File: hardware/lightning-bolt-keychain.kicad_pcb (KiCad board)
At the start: 2 copper layers, 74 x 101 mm, 15 parts, among them J1 USB-C Power

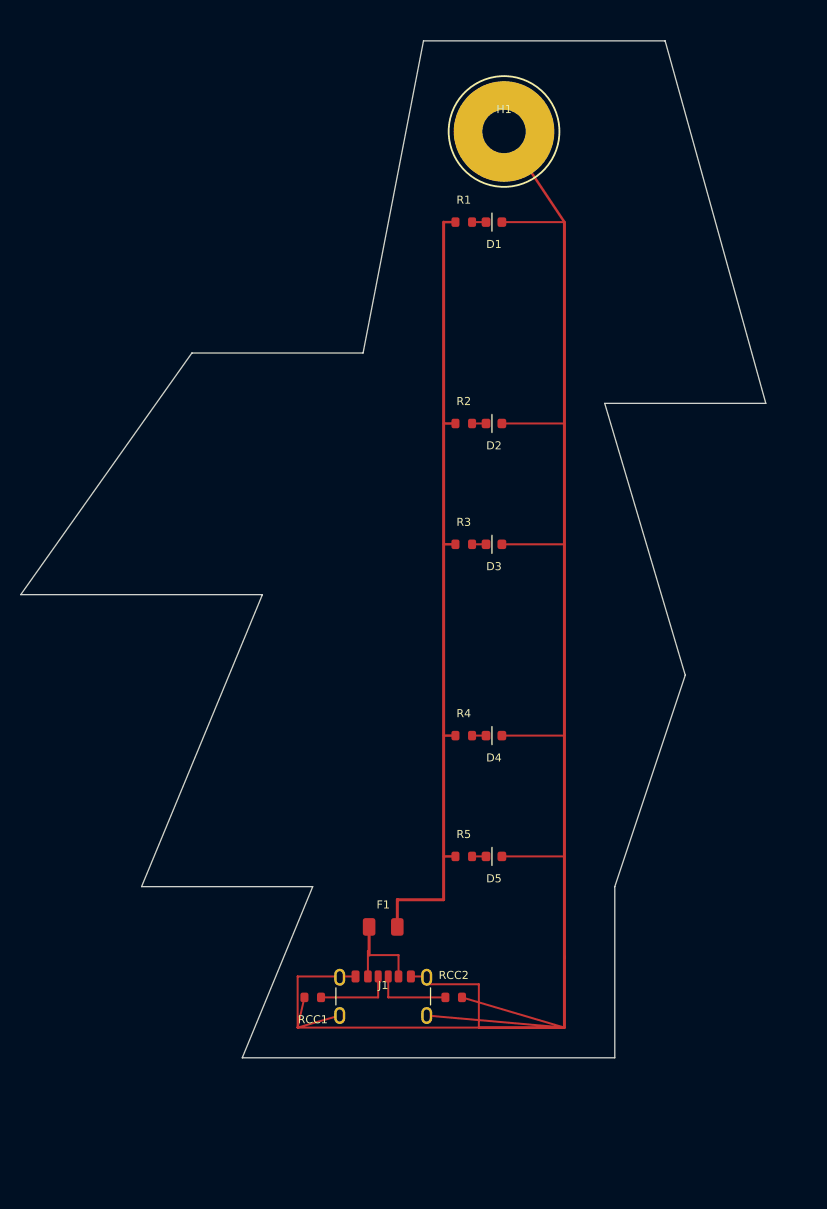
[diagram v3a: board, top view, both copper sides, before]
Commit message: Refine bolt outline and schematic readability
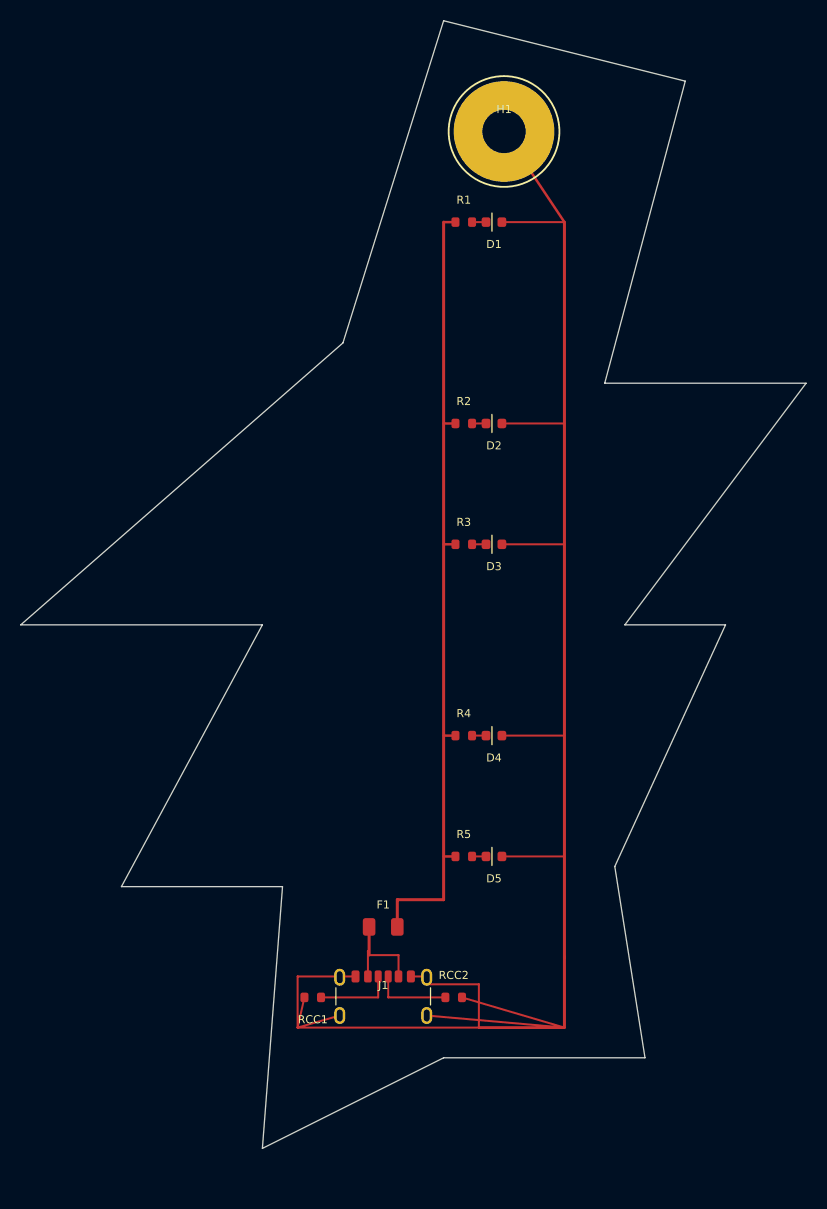
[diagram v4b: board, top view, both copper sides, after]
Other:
- board size 74 x 101 mm -> 78 x 112 mm
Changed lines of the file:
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@@
     (pad "2" smd roundrect (at 0.7875 0) (size 0.875 0.95) (layers "F.Cu" "F.Paste" "F.Mask") (net 10 "LED5") (pinfunction "A") (roundrect_rratio 0.25))
   )
-  (gr_line (start 86 20) (end 110 20) (stroke (width 0.12) (type solid)) (layer "Edge.Cuts"))
-  (gr_line (start 110 20) (end 120 56) (stroke (width 0.12) (type solid)) (layer "Edge.Cuts"))
-  (gr_line (start 120 56) (end 104 56) (stroke (width 0.12) (type solid)) (layer "Edge.Cuts"))
-  (gr_line (start 104 56) (end 112 83) (stroke (width 0.12) (type solid)) (layer "Edge.Cuts"))
-  (gr_line (start 112 83) (end 105 104) (stroke (width 0.12) (type solid)) (layer "Edge.Cuts"))
-  (gr_line (start 105 104) (end 105 121) (stroke (width 0.12) (type solid)) (layer "Edge.Cuts"))
-  (gr_line (start 105 121) (end 68 121) (stroke (width 0.12) (type solid)) (layer "Edge.Cuts"))
-  (gr_line (start 68 121) (end 75 104) (stroke (width 0.12) (type solid)) (layer "Edge.Cuts"))
-  (gr_line (start 75 104) (end 58 104) (stroke (width 0.12) (type solid)) (layer "Edge.Cuts"))
-  (gr_line (start 58 104) (end 70 75) (stroke (width 0.12) (type solid)) (layer "Edge.Cuts"))
-  (gr_line (start 70 75) (end 46 75) (stroke (width 0.12) (type solid)) (layer "Edge.Cuts"))
-  (gr_line (start 46 75) (end 63 51) (stroke (width 0.12) (type solid)) (layer "Edge.Cuts"))
-  (gr_line (start 63 51) (end 80 51) (stroke (width 0.12) (type solid)) (layer "Edge.Cuts"))
-  (gr_line (start 80 51) (end 86 20) (stroke (width 0.12) (type solid)) (layer "Edge.Cuts"))
-  (segment (start 80.48 112.92) (end 80.48 110.4) (width 0.20) (layer "F.Cu") (net 2))
+  (gr_line (start 88 18) (end 112 24) (stroke (width 0.12) (type solid)) (layer "Edge.Cuts"))
+  (gr_line (start 112 24) (end 104 54) (stroke (width 0.12) (type solid)) (layer "Edge.Cuts"))
+  (gr_line (start 104 54) (end 124 54) (stroke (width 0.12) (type solid)) (layer "Edge.Cuts"))
+  (gr_line (start 124 54) (end 106 78) (stroke (width 0.12) (type solid)) (layer "Edge.Cuts"))
+  (gr_line (start 106 78) (end 116 78) (stroke (width 0.12) (type solid)) (layer "Edge.Cuts"))
+  (gr_line (start 116 78) (end 105 102) (stroke (width 0.12) (type solid)) (layer "Edge.Cuts"))
+  (gr_line (start 105 102) (end 108 121) (stroke (width 0.12) (type solid)) (layer "Edge.Cuts"))
+  (gr_line (start 108 121) (end 88 121) (stroke (width 0.12) (type solid)) (layer "Edge.Cuts"))
+  (gr_line (start 88 121) (end 70 130) (stroke (width 0.12) (type solid)) (layer "Edge.Cuts"))
+  (gr_line (start 70 130) (end 72 104) (stroke (width 0.12) (type solid)) (layer "Edge.Cuts"))
+  (gr_line (start 72 104) (end 56 104) (stroke (width 0.12) (type solid)) (layer "Edge.Cuts"))
+  (gr_line (start 56 104) (end 70 78) (stroke (width 0.12) (type solid)) (layer "Edge.Cuts"))
+  (gr_line (start 70 78) (end 46 78) (stroke (width 0.12) (type solid)) (layer "Edge.Cuts"))
+  (gr_line (start 46 78) (end 78 50) (stroke (width 0.12) (type solid)) (layer "Edge.Cuts"))
+  (gr_line (start 78 50) (end 88 18) (stroke (width 0.12) (type solid)) (layer "Edge.Cuts"))  (segment (start 80.48 112.92) (end 80.48 110.4) (width 0.20) (layer "F.Cu") (net 2))
   (segment (start 80.48 110.4) (end 80.6 110.4) (width 0.20) (layer "F.Cu") (net 2))
   (segment (start 83.52 112.92) (end 83.52 110.8) (width 0.20) (layer "F.Cu") (net 2))

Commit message: Refine lightning bolt silhouette
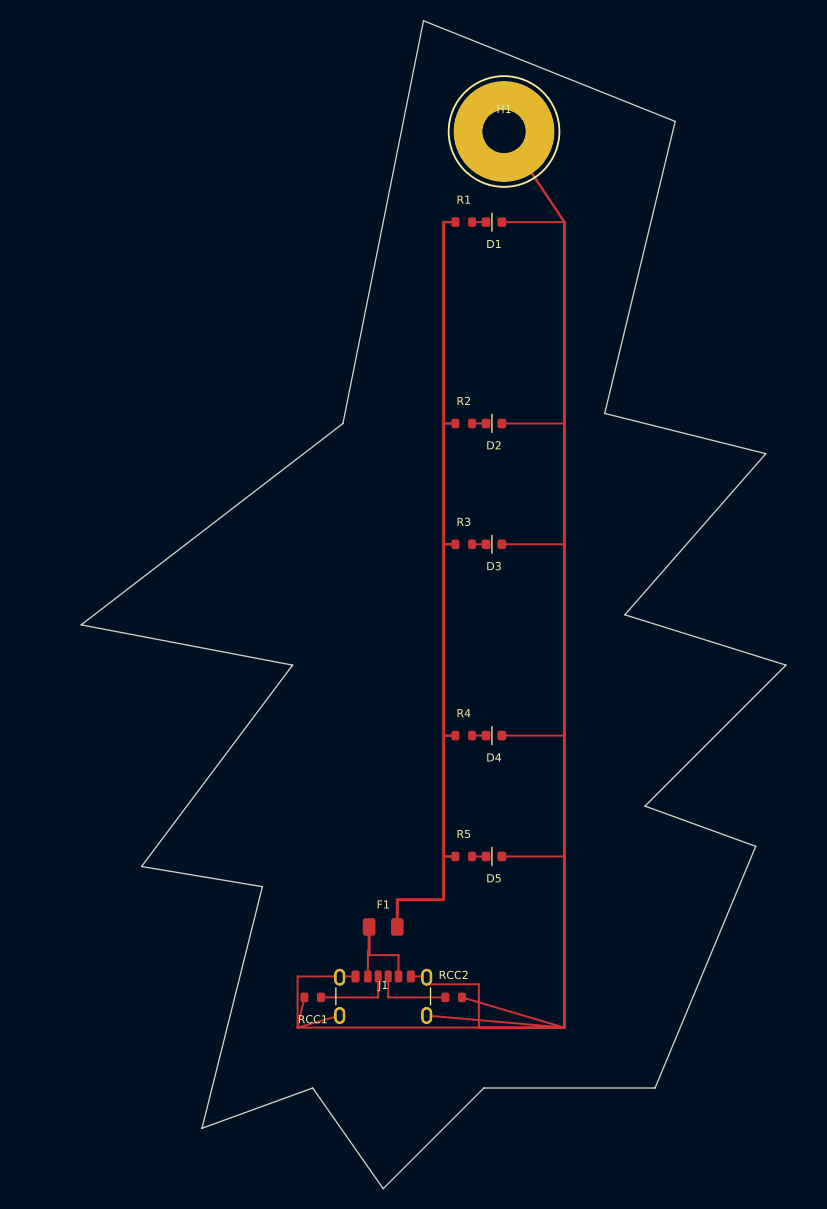
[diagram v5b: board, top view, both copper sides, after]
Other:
- board size 78 x 112 mm -> 70 x 116 mm
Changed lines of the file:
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@@
     (pad "2" smd roundrect (at 0.7875 0) (size 0.875 0.95) (layers "F.Cu" "F.Paste" "F.Mask") (net 10 "LED5") (pinfunction "A") (roundrect_rratio 0.25))
   )
-  (gr_line (start 88 18) (end 112 24) (stroke (width 0.12) (type solid)) (layer "Edge.Cuts"))
-  (gr_line (start 112 24) (end 104 54) (stroke (width 0.12) (type solid)) (layer "Edge.Cuts"))
-  (gr_line (start 104 54) (end 124 54) (stroke (width 0.12) (type solid)) (layer "Edge.Cuts"))
-  (gr_line (start 124 54) (end 106 78) (stroke (width 0.12) (type solid)) (layer "Edge.Cuts"))
-  (gr_line (start 106 78) (end 116 78) (stroke (width 0.12) (type solid)) (layer "Edge.Cuts"))
-  (gr_line (start 116 78) (end 105 102) (stroke (width 0.12) (type solid)) (layer "Edge.Cuts"))
-  (gr_line (start 105 102) (end 108 121) (stroke (width 0.12) (type solid)) (layer "Edge.Cuts"))
-  (gr_line (start 108 121) (end 88 121) (stroke (width 0.12) (type solid)) (layer "Edge.Cuts"))
-  (gr_line (start 88 121) (end 70 130) (stroke (width 0.12) (type solid)) (layer "Edge.Cuts"))
-  (gr_line (start 70 130) (end 72 104) (stroke (width 0.12) (type solid)) (layer "Edge.Cuts"))
-  (gr_line (start 72 104) (end 56 104) (stroke (width 0.12) (type solid)) (layer "Edge.Cuts"))
-  (gr_line (start 56 104) (end 70 78) (stroke (width 0.12) (type solid)) (layer "Edge.Cuts"))
-  (gr_line (start 70 78) (end 46 78) (stroke (width 0.12) (type solid)) (layer "Edge.Cuts"))
-  (gr_line (start 46 78) (end 78 50) (stroke (width 0.12) (type solid)) (layer "Edge.Cuts"))
-  (gr_line (start 78 50) (end 88 18) (stroke (width 0.12) (type solid)) (layer "Edge.Cuts"))  (segment (start 80.48 112.92) (end 80.48 110.4) (width 0.20) (layer "F.Cu") (net 2))
+  (gr_line (start 86 18) (end 111 28) (stroke (width 0.12) (type solid)) (layer "Edge.Cuts"))
+  (gr_line (start 111 28) (end 104 57) (stroke (width 0.12) (type solid)) (layer "Edge.Cuts"))
+  (gr_line (start 104 57) (end 120 61) (stroke (width 0.12) (type solid)) (layer "Edge.Cuts"))
+  (gr_line (start 120 61) (end 106 77) (stroke (width 0.12) (type solid)) (layer "Edge.Cuts"))
+  (gr_line (start 106 77) (end 122 82) (stroke (width 0.12) (type solid)) (layer "Edge.Cuts"))
+  (gr_line (start 122 82) (end 108 96) (stroke (width 0.12) (type solid)) (layer "Edge.Cuts"))
+  (gr_line (start 108 96) (end 119 100) (stroke (width 0.12) (type solid)) (layer "Edge.Cuts"))
+  (gr_line (start 119 100) (end 109 124) (stroke (width 0.12) (type solid)) (layer "Edge.Cuts"))
+  (gr_line (start 109 124) (end 92 124) (stroke (width 0.12) (type solid)) (layer "Edge.Cuts"))
+  (gr_line (start 92 124) (end 82 134) (stroke (width 0.12) (type solid)) (layer "Edge.Cuts"))
+  (gr_line (start 82 134) (end 75 124) (stroke (width 0.12) (type solid)) (layer "Edge.Cuts"))
+  (gr_line (start 75 124) (end 64 128) (stroke (width 0.12) (type solid)) (layer "Edge.Cuts"))
+  (gr_line (start 64 128) (end 70 104) (stroke (width 0.12) (type solid)) (layer "Edge.Cuts"))
+  (gr_line (start 70 104) (end 58 102) (stroke (width 0.12) (type solid)) (layer "Edge.Cuts"))
+  (gr_line (start 58 102) (end 73 82) (stroke (width 0.12) (type solid)) (layer "Edge.Cuts"))
+  (gr_line (start 73 82) (end 52 78) (stroke (width 0.12) (type solid)) (layer "Edge.Cuts"))
+  (gr_line (start 52 78) (end 78 58) (stroke (width 0.12) (type solid)) (layer "Edge.Cuts"))
+  (gr_line (start 78 58) (end 86 18) (stroke (width 0.12) (type solid)) (layer "Edge.Cuts"))  (segment (start 80.48 112.92) (end 80.48 110.4) (width 0.20) (layer "F.Cu") (net 2))
   (segment (start 80.48 110.4) (end 80.6 110.4) (width 0.20) (layer "F.Cu") (net 2))
   (segment (start 83.52 112.92) (end 83.52 110.8) (width 0.20) (layer "F.Cu") (net 2))

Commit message: Sharpen slim lightning bolt PCB outline
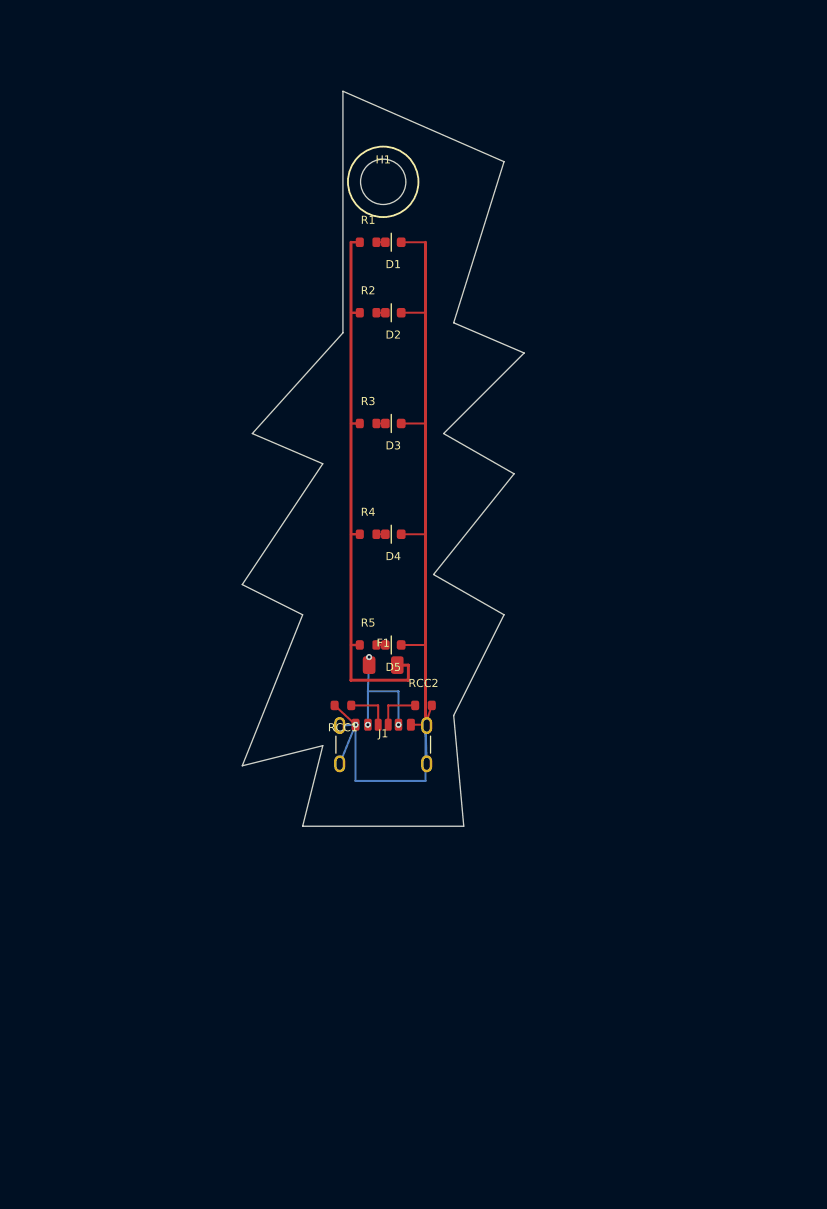
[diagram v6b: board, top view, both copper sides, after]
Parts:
- moved RCC1 29.2 mm to (78.0, 86.0)
- moved RCC2 29.2 mm to (86.0, 86.0)
- moved F1 26.0 mm to (82.0, 82.0)
- moved J1 25.0 mm to (82.0, 91.0)
- moved D5 23.3 mm to (83.0, 80.0)
- moved R5 23.0 mm to (80.5, 80.0)
- moved D4 22.4 mm to (83.0, 69.0)
- moved R4 22.1 mm to (80.5, 69.0)
- moved D3 15.6 mm to (83.0, 58.0)
- moved R3 15.3 mm to (80.5, 58.0)
- moved D2 14.9 mm to (83.0, 47.0)
- moved R2 14.5 mm to (80.5, 47.0)
- moved H1 13.0 mm to (82.0, 34.0)
- moved D1 10.2 mm to (83.0, 40.0)
- moved R1 9.71 mm to (80.5, 40.0)
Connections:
- H1 pad 1: GND -> (no net)
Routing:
- net GND: track 211.6 -> 94.2 mm, vias 0 -> 2
- net VLED: track 80.5 -> 56.2 mm
- net VBUS: track 10.5 -> 13.9 mm, vias 0 -> 3
- net CC2: track 7.75 -> 4.59 mm
- net CC1: track 7.75 -> 4.59 mm
- net LED5: track 1.39 -> 0.89 mm
- net LED4: track 1.39 -> 0.89 mm
- net LED3: track 1.39 -> 0.89 mm
- net LED2: track 1.39 -> 0.89 mm
- net LED1: track 1.39 -> 0.89 mm
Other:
- board size 70 x 116 mm -> 28 x 73 mm
